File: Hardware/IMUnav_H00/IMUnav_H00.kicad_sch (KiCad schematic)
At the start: 1 part, among them U1 STM32G474VETx

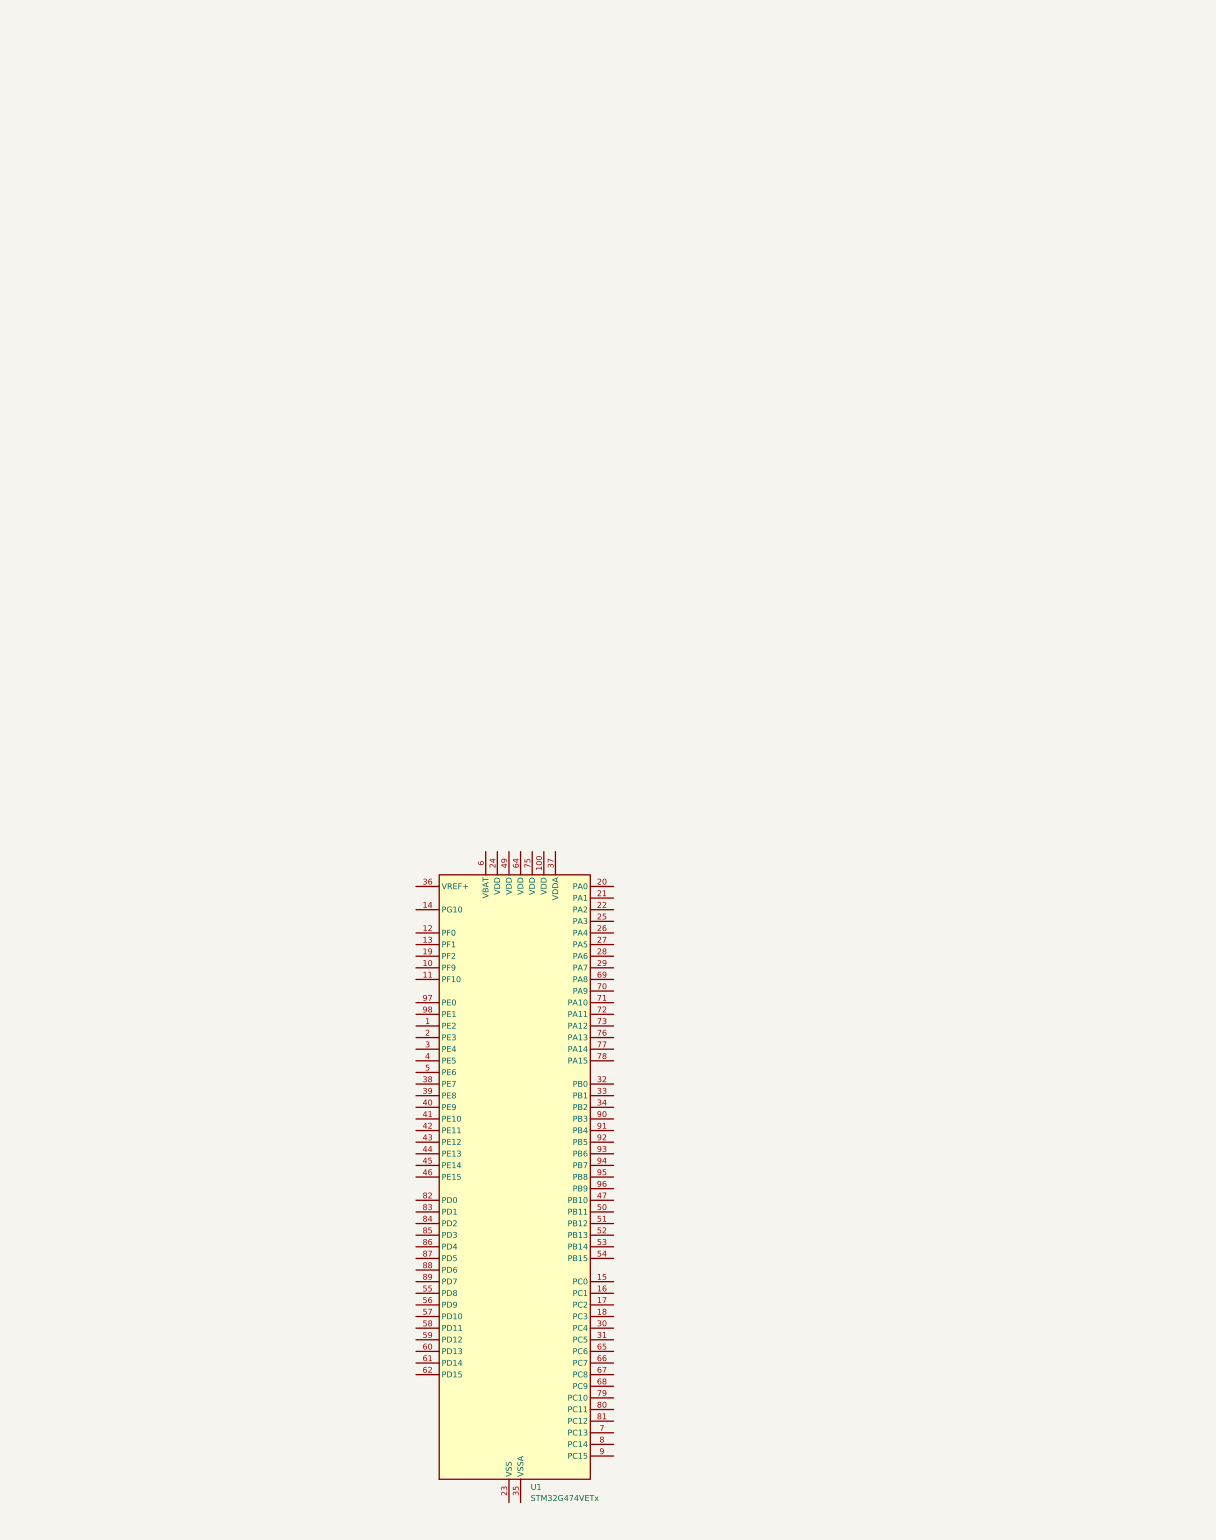
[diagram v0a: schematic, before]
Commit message: HW design - USB, ESP, DC/DC converter
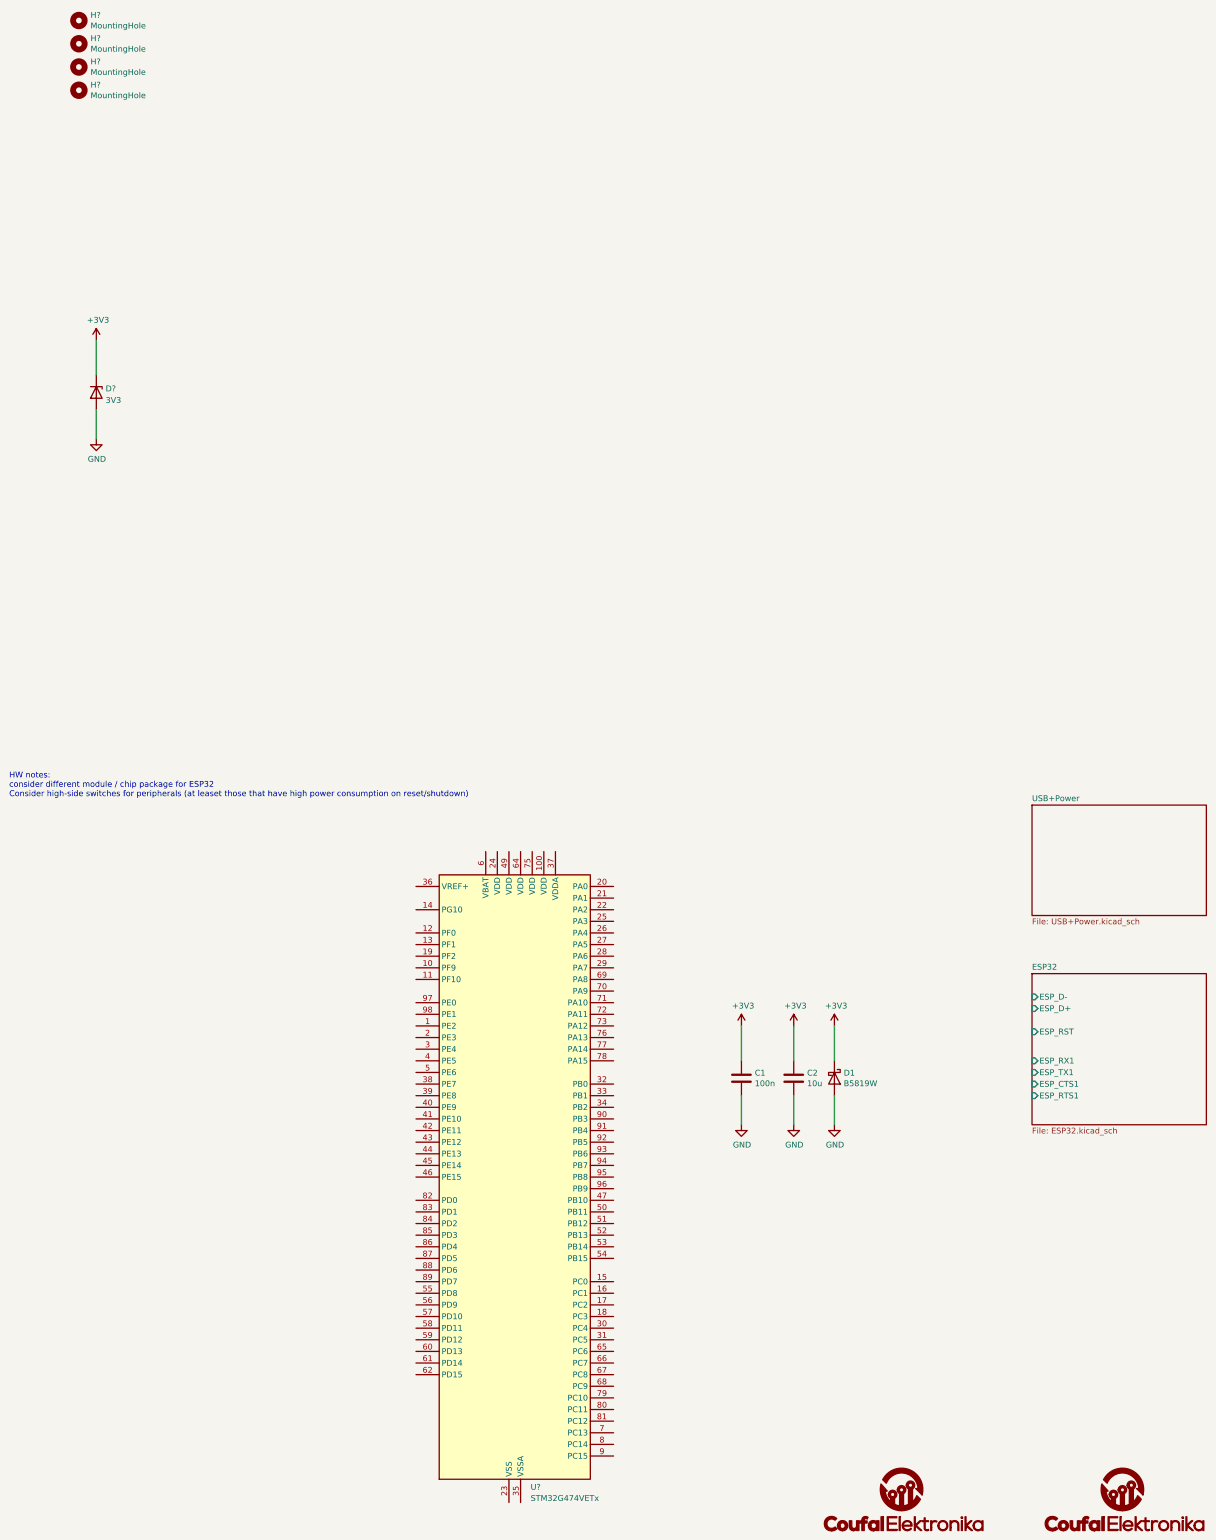
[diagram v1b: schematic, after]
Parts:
- added C1: 100n, Capacitor_SMD:C_0603_1608Metric, symbol Device:C
- added C2: 10u, Capacitor_SMD:C_0805_2012Metric, symbol Device:C
- added D1: B5819W, Diode_SMD:D_SOD-123, symbol Device:D_Schottky
- added D?: 3V3, Diode_SMD:D_MiniMELF, symbol Device:D_Zener
- added G?: CoufalElektronika_logo, PaLampa_Library:Coufal_elektronika_text_30x13mm, symbol Time-O-Mat_Library:CoufalElektronika_logo
- added G?: CoufalElektronika_logo, PaLampa_Library:Coufal_elektronika_notext_10mm, symbol Time-O-Mat_Library:CoufalElektronika_logo
- added H? (x4): MountingHole, MountingHole:MountingHole_3.2mm_M3, symbol Mechanical:MountingHole
- renumbered U1 to U?
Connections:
- new net +3V3: C1.1, C2.1, D1.1 (K), D?.1 (K)
- new net GND: C1.2, C2.2, D1.2 (A), D?.2 (A)
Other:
- added sheet ESP32 (ESP32.kicad_sch)
- added sheet USB+Power (USB+Power.kicad_sch)
- note added: "HW notes: consider different module / chip package for ESP32 Consider high-side switches for peripherals (at leaset those that have high power consumption on reset/shutdown)"

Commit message: Finished USB Hub connection, added battery and power management. Added sheets for IMU and GPS.
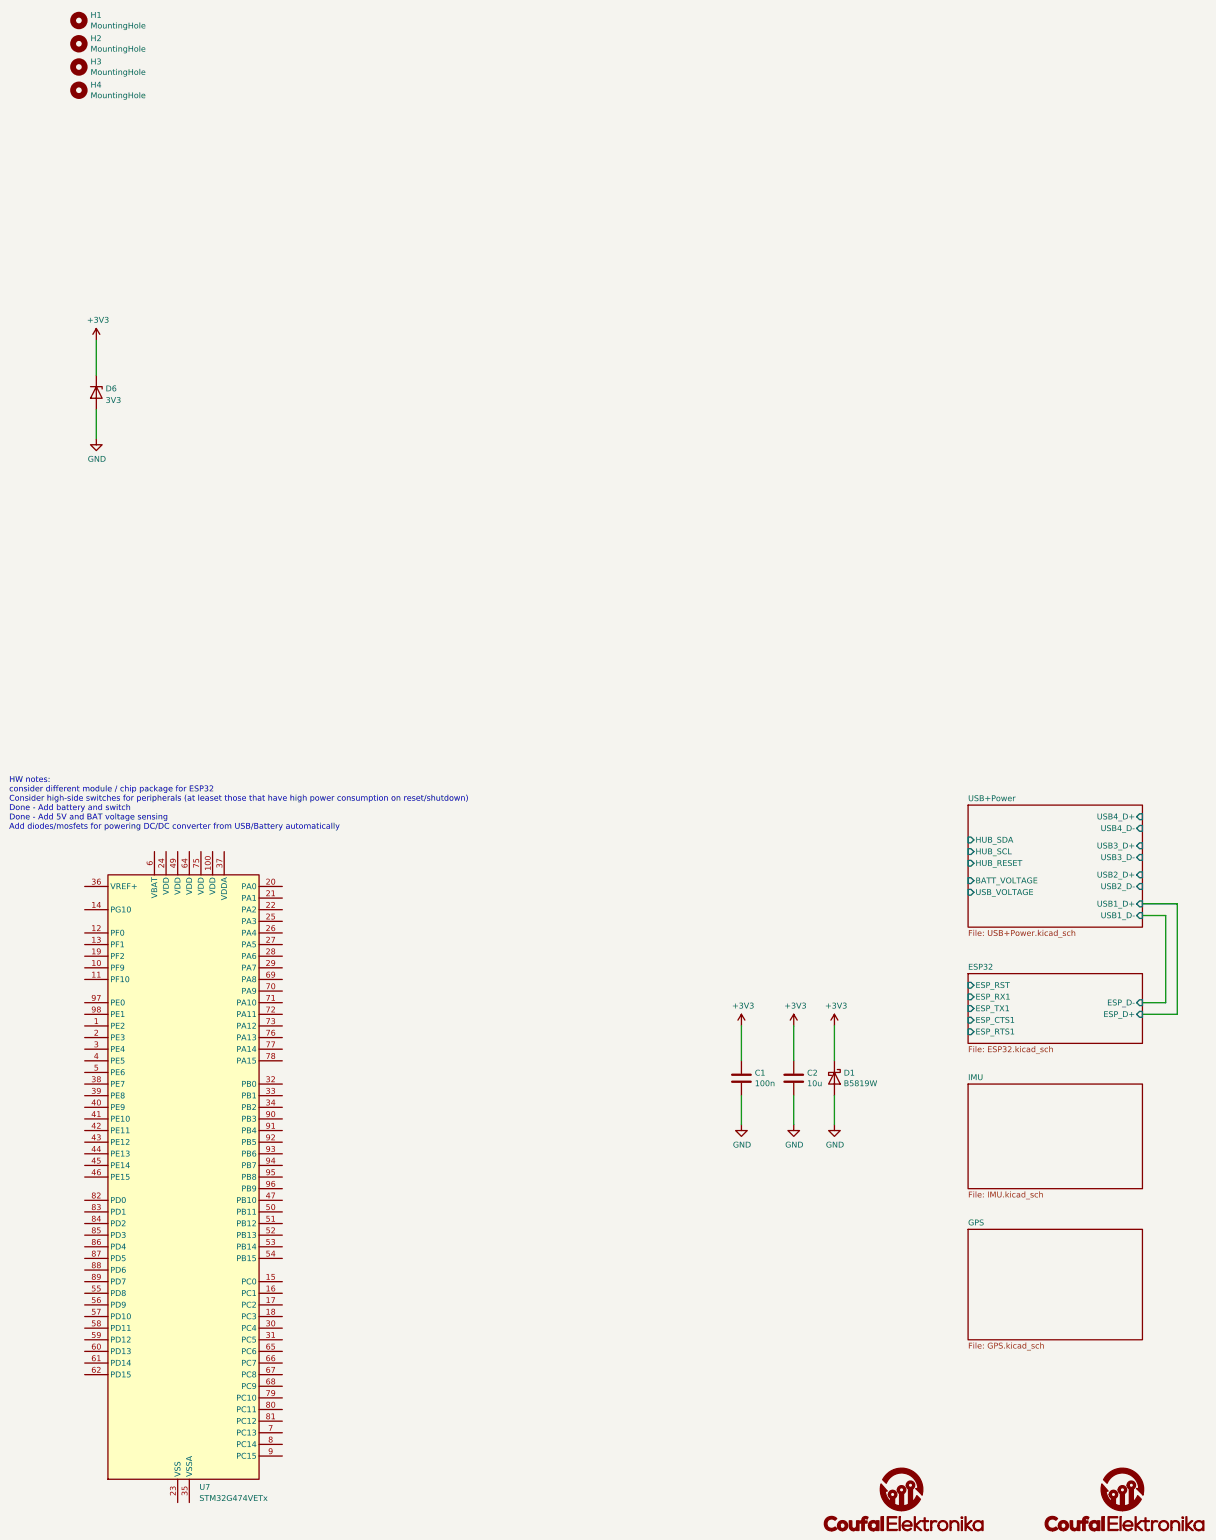
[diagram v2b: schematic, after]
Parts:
- gave numbers to parts that had none: 6
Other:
- added sheet GPS (GPS.kicad_sch)
- added sheet IMU (IMU.kicad_sch)
- sheet USB+Power ports: added BATT_VOLTAGE, HUB_RESET, HUB_SCL, HUB_SDA, USB1_D+, USB1_D-, USB2_D+, USB2_D-, USB3_D+, USB3_D-, USB4_D+, USB4_D-, USB_VOLTAGE; removed none
- note added: "HW notes: consider different module / chip package for ESP32 Consider high-side switches for peripherals (at leaset those that have high power consumption on reset/shutdown) Done - Add battery and switch Done - Add 5V and BAT voltage sensing Add diodes/mosfets for powering DC/DC converter from USB/Battery automatically"
- note removed: "HW notes: consider different module / chip package for ESP32 Consider high-side switches for peripherals (at leaset those that have high power consumption on reset/shutdown)"
- moved on the sheet: U7
